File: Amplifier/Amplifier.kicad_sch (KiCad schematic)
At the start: 47 parts, among them J1 132365-10, J2 SMA-J-P-H-ST-EM1, J3 JST_VH, U1 SKY65111-348LF, U2 MAX2633EUT+T, U3 RLM-23-1WL+, U4 SKYA21001, U5 SKYA21001, U6 TPS63051RMWR

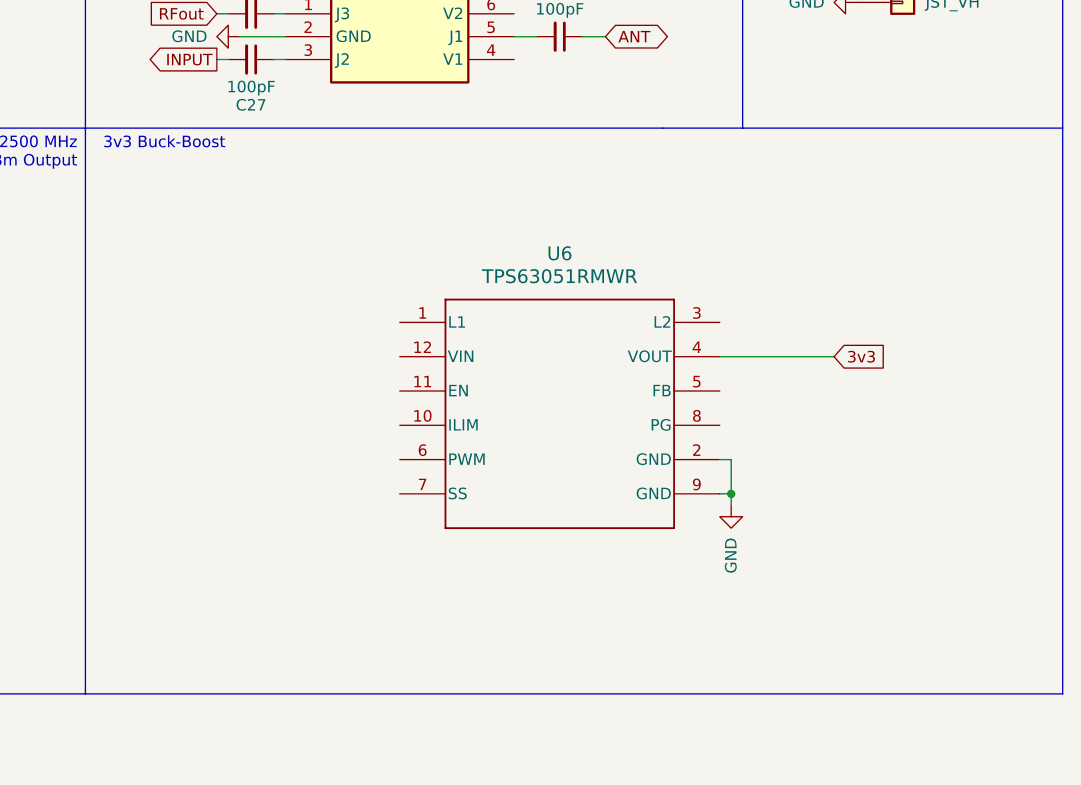
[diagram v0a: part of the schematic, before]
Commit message: added/updated caps/inductor for 3v3 reg. updated pcb layout. updated footprints for connectors. started adding fence vias.
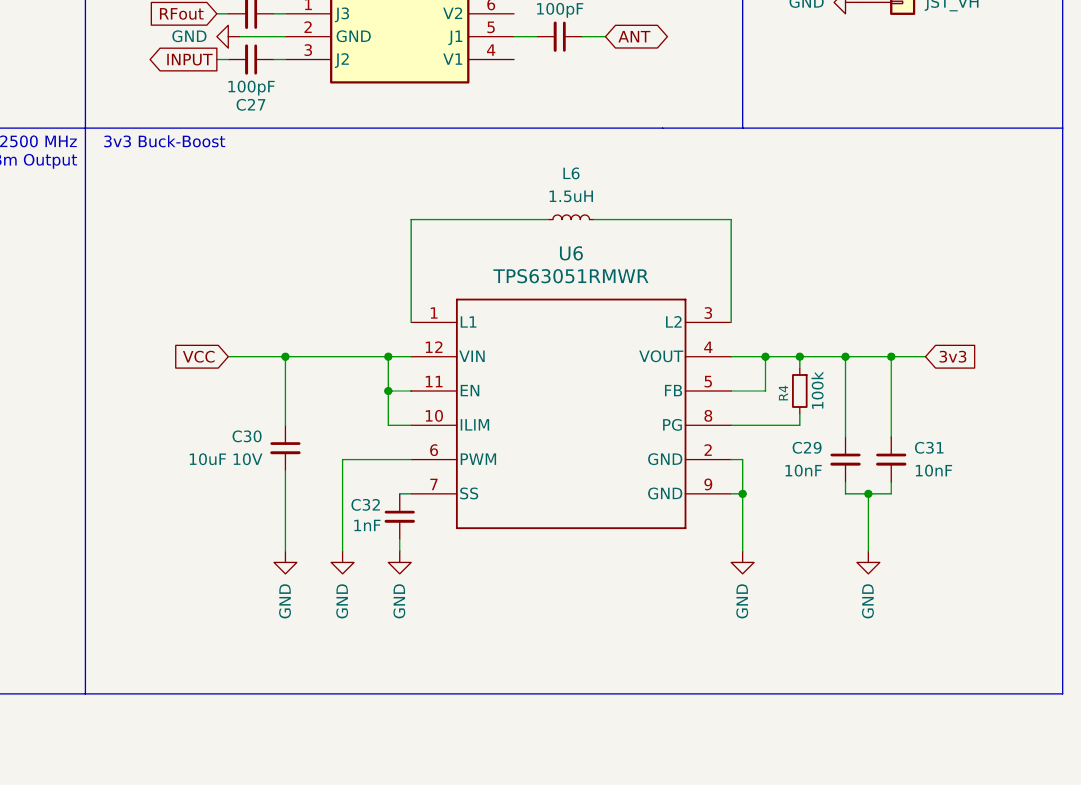
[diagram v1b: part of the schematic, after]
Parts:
- added C29, C31: 10nF, Capacitor_SMD:C_0603_1608Metric, symbol amp:10uF 6.3V
- added C30: 10uF 10V, Capacitor_SMD:C_0603_1608Metric, symbol Device:C_Small
- added C32: 1nF, Capacitor_SMD:C_0402_1005Metric, symbol amp:1nF 10V
- added L6: 1.5uH, Inductor_SMD:L_1008_2520Metric, symbol amp:1.5uH
- added R4: 100k, Resistor_SMD:R_0603_1608Metric, symbol Device:R_Small
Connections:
- net 3v3: now also U6.5 (FB), C29.1, C31.1, R4.1
- net GND: now also U6.6 (PWM), C29.2, C30.2, C31.2, C32.2
- net VCC: now also U6.10 (ILIM), U6.11 (EN), U6.12 (VIN), C30.1
- net at U6.1 (L1): now also L6.1
- net at U6.3 (L2): now also L6.2
- net at U6.7 (SS): now also C32.1
- net at U6.8 (PG): now also R4.2
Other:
- moved on the sheet: U6

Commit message: updated note in schematic. updated PCB ground vias/fencing
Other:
- note added: "NOTES: 1. For use with LILYGO T-Beam Supreme - 915MHz 2. 3. 4. Pretend I didn't work out of main"
- note removed: "NOTES: 1. 2. 3. 4. Pretend I didn't work out of main"
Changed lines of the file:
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@@
 		)
 	)
-	(text "NOTES:\n1.\n2.\n3.\n4. Pretend I didn't work out of main"
+	(text "NOTES:\n1. For use with LILYGO T-Beam Supreme - 915MHz\n2. \n3. \n4. Pretend I didn't work out of main"
 		(exclude_from_sim no)
 		(at 19.05 184.912 0)
